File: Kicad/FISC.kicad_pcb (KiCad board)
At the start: 2 copper layers, 229.2 x 95.4 mm, 59 parts, among them IC1 DS1233-10+, J1 Data Bus Pin Header, J2 Address Bus Pin Header, J3 uSeq Pin Header, J4 Control Lines Pin Header, J5 Clock Pin Header, SW1 SW_Push, U1 74LS593, U10 AT28C64B, U11 74HCT574, U12 74HCT574, U13 74HCT574, U14 74HCT574, U15 74HCT541, U16 74HCT541, U17 74HCT574, U18 74HCT161, U19 74HCT138, U2 74LS593, U20 74HCT151, U21 74HCT139, U22 74HCT154, U23 M27C322-100F1, U24 UM245R, U25 AT27C1024-70PU, U26 ECS-100AX-035, U3 74HCT138, U4 74HCT240, U5 74LS469, U6 74LS469, U7 74HCT574, U8 74HCT574, U9 AS6C1008

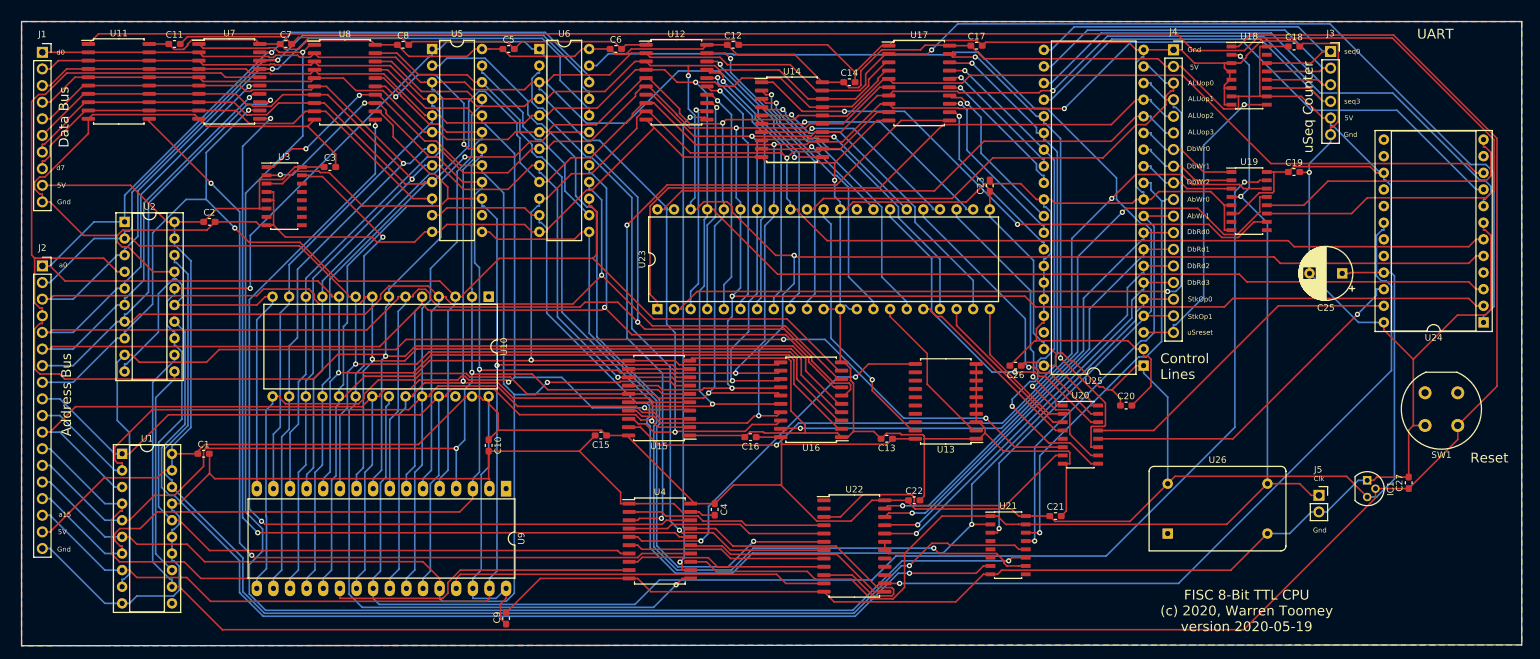
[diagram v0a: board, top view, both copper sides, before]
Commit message: Lots of changes.
I found a few wiring mistakes in the schematic and fixed them up.
I added microcode instructions to allow B to be copied out to A,
to the UART and to memory. I added a lot of `mem = mem op B`
instructions. I added some examples to test the above. I redid the
PCB layout and added copper pours.
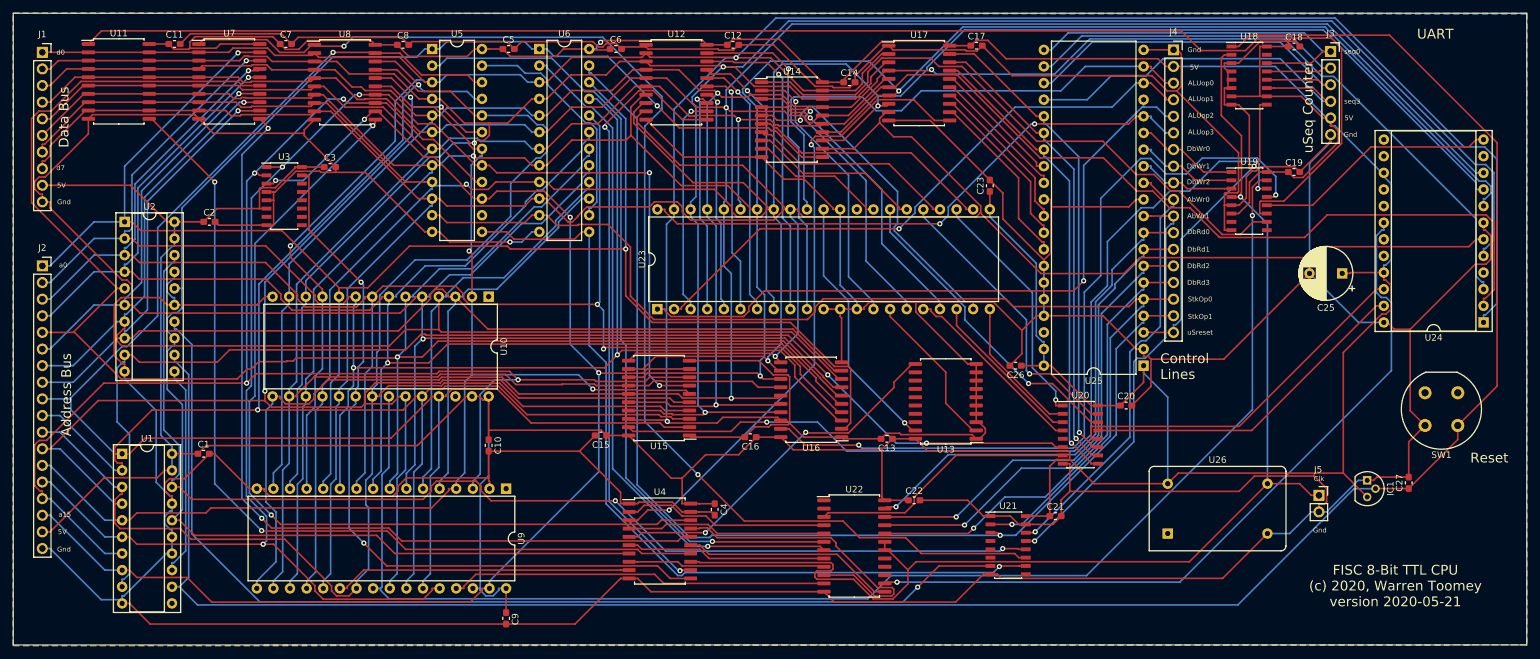
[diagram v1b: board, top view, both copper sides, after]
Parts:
- U9: footprint Package_DIP:DIP-32_W15.24mm_LongPads -> Package_DIP:DIP-32_W15.24mm
- turned C9 to 270 degrees
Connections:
- U21 pad 1: Clk -> Lo
- U21 pad 15: Clk -> Lo
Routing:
- net Lo: track 1222.7 -> 1329.7 mm, vias 2 -> 1
- net adr3: track 302.1 -> 246.7 mm
- net ~Awrite: track 267.6 -> 228.6 mm
- net d3: track 398.5 -> 435.6 mm
- net ~ARwrite: track 230.0 -> 194.3 mm
- net adr2: track 275.9 -> 240.9 mm, vias 2 -> 3
- net d6: track 405.8 -> 436.4 mm
- net adr14: track 201.4 -> 231.1 mm, vias 3 -> 4
- net d4: track 404.9 -> 434.4 mm, vias 4 -> 1
- net adr11: track 205.2 -> 233.7 mm, vias 1 -> 3
- net adr4: track 252.3 -> 279.4 mm, vias 2 -> 1
- net d1: track 412.4 -> 439.2 mm
- net d0: track 429.2 -> 455.1 mm, vias 2 -> 3
- net adr7: track 215.0 -> 236.8 mm, vias 2 -> 1
- net ALUop1: track 114.1 -> 92.5 mm
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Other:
- board size 229.2 x 95.4 mm -> 231.3 x 96.5 mm
- board text added: "FISC 8-Bit TTL CPU (c) 2020, Warren Toomey version 2020-05-21"
- board text removed: "FISC 8-Bit TTL CPU (c) 2020, Warren Toomey version 2020-05-19"
